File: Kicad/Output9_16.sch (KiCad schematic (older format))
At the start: 20 parts, among them J10 String10, J11 String11, J12 String12, J13 String13, J14 String14, J15 String15, J16 String16, J9 String9, U4 SN74HCT245N

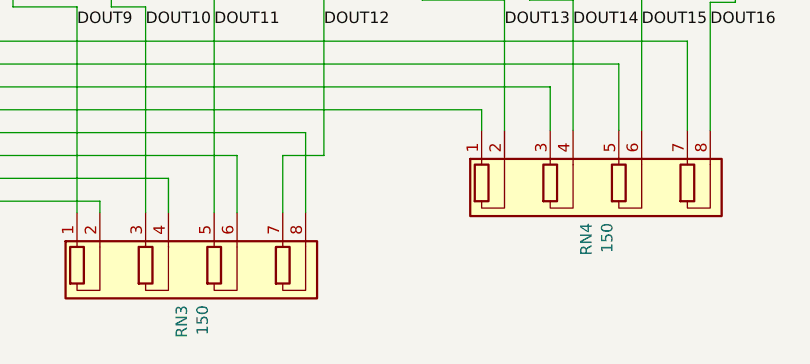
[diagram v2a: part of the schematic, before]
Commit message: updated PB16 to rev G, changed power in ports to screw type connector
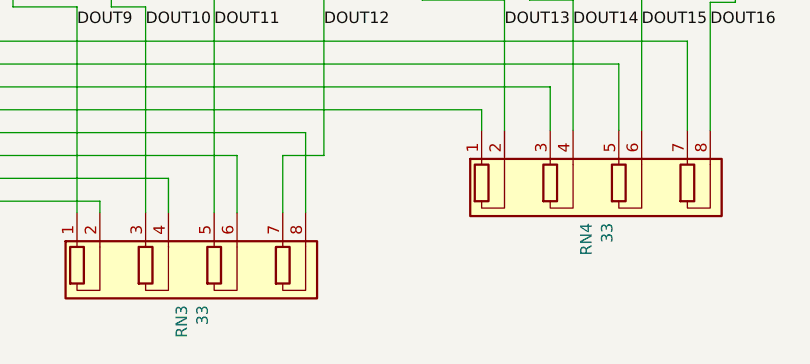
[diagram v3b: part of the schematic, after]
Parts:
- RN3, RN4: value 150 -> 33; Digi-Key_PN 4608X-2-151LF-ND -> 4608X-2-330LF-ND; MPN 4608X-102-151LF -> 4608X-102-330LF
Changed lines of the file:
@@
 EESchema Schematic File Version 4
-LIBS:PB_16-cache
 EELAYER 30 0
 EELAYER END
@@
 Sheet 4 5
 Title "PB 16"
-Date "2019-10-07"
-Rev "v1.0f"
+Date "2020-05-09"
+Rev "v1.0g"
 Comp "Scott Hanson"
 Comment1 ""
@@
 AR Path="/5D4698DE/5D4E3AEB" Ref="RN4"  Part="1"
 F 0 "RN4" V 8658 5115 50  0000 L CNN
-F 1 "150" V 8749 5115 50  0000 L CNN
+F 1 "33" V 8749 5115 50  0000 L CNN
 F 2 "Resistor_THT:R_Array_SIP8" V 9375 4910 50  0001 C CNN
 F 3 "http://www.vishay.com/docs/31509/csc.pdf" H 8700 4910 50  0001 C CNN
-F 4 "4608X-2-151LF-ND" H -960 -120 50  0001 C CNN "Digi-Key_PN"
-F 5 "4608X-102-151LF" H -960 -120 50  0001 C CNN "MPN"
+F 4 "4608X-2-330LF-ND" H -960 -120 50  0001 C CNN "Digi-Key_PN"
+F 5 "4608X-102-330LF" H -960 -120 50  0001 C CNN "MPN"
 	1    8700 4910
 	1    0    0    1
@@
 AR Path="/5D4698DE/5D4E3B1E" Ref="RN3"  Part="1"
 F 0 "RN3" V 6888 5475 50  0000 L CNN
-F 1 "150" V 6979 5475 50  0000 L CNN
+F 1 "33" V 6979 5475 50  0000 L CNN
 F 2 "Resistor_THT:R_Array_SIP8" V 7605 5270 50  0001 C CNN
 F 3 "http://www.vishay.com/docs/31509/csc.pdf" H 6930 5270 50  0001 C CNN
-F 4 "4608X-2-151LF-ND" H -760 280 50  0001 C CNN "Digi-Key_PN"
-F 5 "4608X-102-151LF" H -760 280 50  0001 C CNN "MPN"
+F 4 "4608X-2-330LF-ND" H -760 280 50  0001 C CNN "Digi-Key_PN"
+F 5 "4608X-102-330LF" H -760 280 50  0001 C CNN "MPN"
 	1    6930 5270
 	1    0    0    1

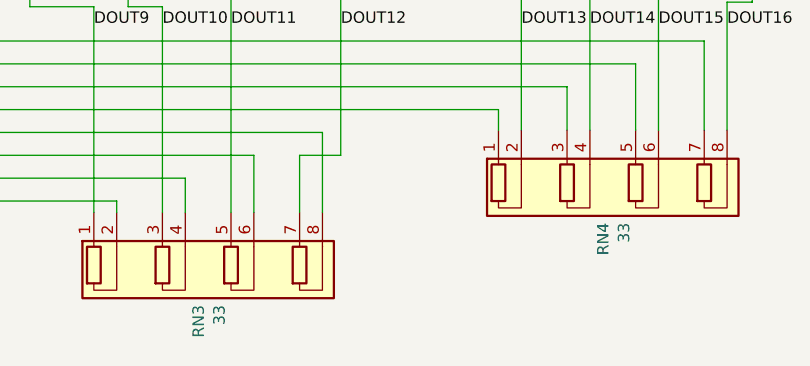
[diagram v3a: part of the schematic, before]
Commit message: cleaning up schematic
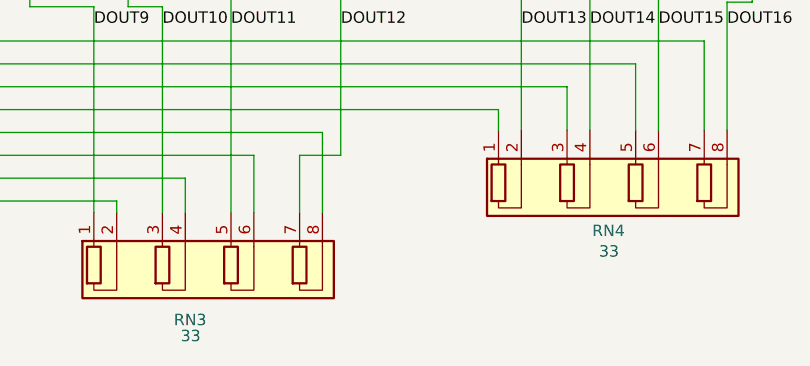
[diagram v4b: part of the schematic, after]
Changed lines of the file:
@@
 AR Path="/5D4E3AEB" Ref="RN?"  Part="1"
 AR Path="/5D4698DE/5D4E3AEB" Ref="RN4"  Part="1"
-F 0 "RN4" V 8658 5115 50  0000 L CNN
-F 1 "33" V 8749 5115 50  0000 L CNN
+F 0 "RN4" H 8610 5150 50  0000 L CNN
+F 1 "33" H 8640 5240 50  0000 L CNN
 F 2 "Resistor_THT:R_Array_SIP8" V 9375 4910 50  0001 C CNN
 F 3 "http://www.vishay.com/docs/31509/csc.pdf" H 8700 4910 50  0001 C CNN
@@
 AR Path="/5D4E3B1E" Ref="RN?"  Part="1"
 AR Path="/5D4698DE/5D4E3B1E" Ref="RN3"  Part="1"
-F 0 "RN3" V 6888 5475 50  0000 L CNN
-F 1 "33" V 6979 5475 50  0000 L CNN
+F 0 "RN3" H 6780 5540 50  0000 L CNN
+F 1 "33" H 6810 5610 50  0000 L CNN
 F 2 "Resistor_THT:R_Array_SIP8" V 7605 5270 50  0001 C CNN
 F 3 "http://www.vishay.com/docs/31509/csc.pdf" H 6930 5270 50  0001 C CNN
